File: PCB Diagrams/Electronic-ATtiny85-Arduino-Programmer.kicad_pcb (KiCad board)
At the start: 2 copper layers, 48.3 x 40.6 mm, 6 parts, among them J1 POWER, J2 01x03, J3 01x01, U1 Arduino Nano v3.x, U2 ATtiny85

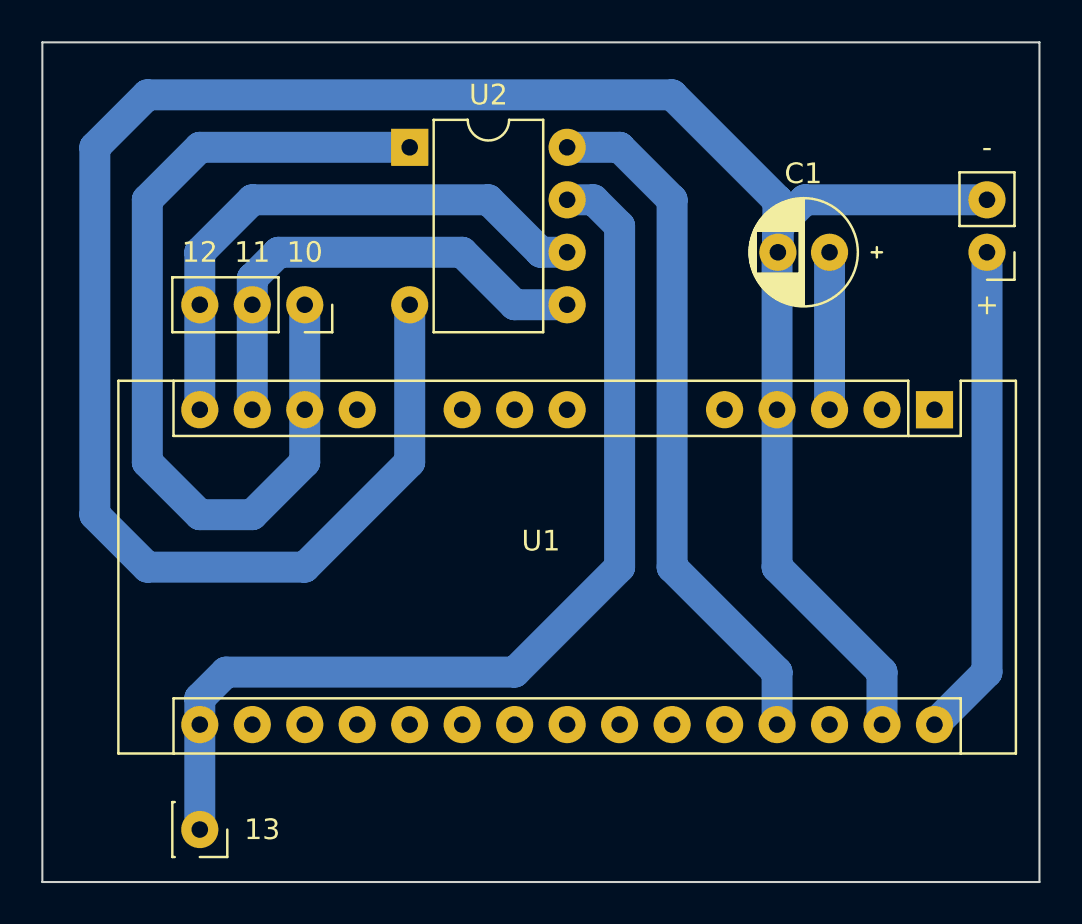
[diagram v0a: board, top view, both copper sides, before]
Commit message: optimizing PCB size
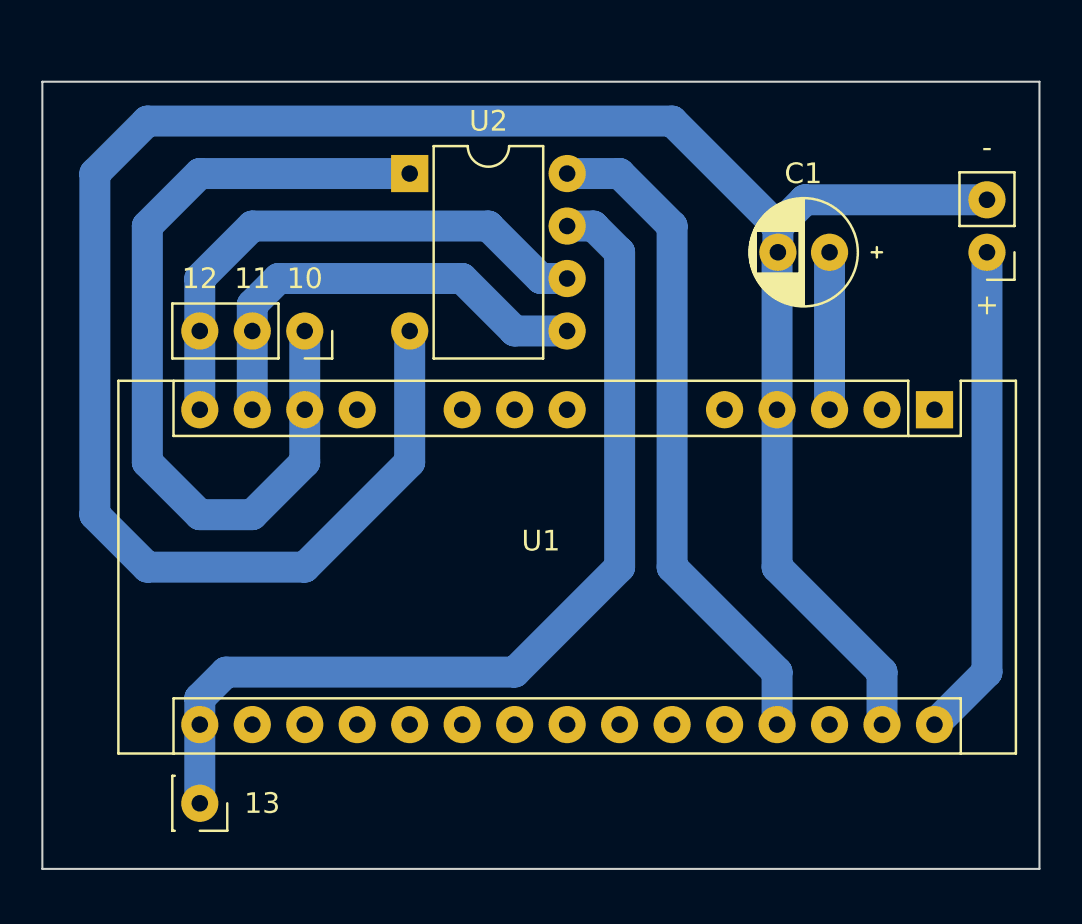
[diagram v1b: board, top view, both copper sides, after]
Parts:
- moved J2 1.27 mm to (137.2, 90.2)
- moved J3 1.27 mm to (132.1, 113.0)
- moved U2 1.27 mm to (142.2, 82.5)
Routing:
- net GND: track 119.4 -> 114.4 mm
- net Net-(J3-Pad1): track 48.9 -> 46.3 mm
- net Net-(J2-Pad1): track 43.8 -> 41.3 mm
- net Net-(J2-Pad2): track 23.2 -> 21.9 mm
- net Net-(J2-Pad3): track 27.5 -> 26.2 mm
- net Net-(U1-Pad27): track 33.6 -> 32.4 mm
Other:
- board size 48.3 x 40.6 mm -> 48.3 x 38.1 mm
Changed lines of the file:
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@@
   (net 26 "Net-(J3-Pad1)")
   (footprint "Connector_PinSocket_2.54mm:PinSocket_1x01_P2.54mm_Vertical" (layer "F.Cu")
-    (at 132.08 114.3 -90)
+    (at 132.08 113.03 -90)
     (descr "Through hole straight socket strip, 1x01, 2.54mm pitch, single row (from Kicad 4.0.7), script generated")
     (tags "Through hole socket strip THT 1x01 2.54mm single row")
@@
   )
   (footprint "Package_DIP:DIP-8_W7.62mm" (layer "F.Cu")
-    (at 142.24 81.28)
+    (at 142.24 82.55)
     (descr "8-lead though-hole mounted DIP package, row spacing 7.62 mm (300 mils)")
     (tags "THT DIP DIL PDIP 2.54mm 7.62mm 300mil")
@@
   )
   (footprint "Connector_PinSocket_2.54mm:PinSocket_1x03_P2.54mm_Vertical" (layer "F.Cu")
-    (at 137.16 88.9 -90)
+    (at 137.16 90.17 -90)
     (descr "Through hole straight socket strip, 1x03, 2.54mm pitch, single row (from Kicad 4.0.7), script generated")
     (tags "Through hole socket strip THT 1x03 2.54mm single row")
@@
     )
   )
-  (gr_line (start 124.46 76.2) (end 124.46 116.84) (layer "Edge.Cuts") (width 0.1))
-  (gr_line (start 172.72 76.2) (end 124.46 76.2) (layer "Edge.Cuts") (width 0.1))
-  (gr_line (start 124.46 116.84) (end 172.72 116.84) (layer "Edge.Cuts") (width 0.1))
-  (gr_line (start 172.72 116.84) (end 172.72 76.2) (layer "Edge.Cuts") (width 0.1))
-  (gr_text "12" (at 132.08 86.36) (layer "F.SilkS")
+  (gr_line (start 124.46 78.105) (end 124.46 116.205) (layer "Edge.Cuts") (width 0.1))
+  (gr_line (start 172.72 78.105) (end 124.46 78.105) (layer "Edge.Cuts") (width 0.1))
+  (gr_line (start 124.46 116.205) (end 172.72 116.205) (layer "Edge.Cuts") (width 0.1))
+  (gr_line (start 172.72 116.205) (end 172.72 78.105) (layer "Edge.Cuts") (width 0.1))
+  (gr_text "12" (at 132.08 87.63) (layer "F.SilkS")
     (effects (font (size 1 1) (thickness 0.2)))
   )
@@
     (effects (font (size 1 1) (thickness 0.2)))
   )
-  (gr_text "11" (at 134.62 86.36) (layer "F.SilkS")
+  (gr_text "11" (at 134.62 87.63) (layer "F.SilkS")
     (effects (font (size 1 1) (thickness 0.2)))
   )
@@
     (effects (font (size 1 1) (thickness 0.2)))
   )
-  (gr_text "13" (at 135.1 114.3) (layer "F.SilkS")
-    (effects (font (size 1 1) (thickness 0.2)))
-  )
-  (gr_text "10" (at 137.16 86.36) (layer "F.SilkS")
+  (gr_text "13" (at 135.1 113.03) (layer "F.SilkS")
+    (effects (font (size 1 1) (thickness 0.2)))
+  )
+  (gr_text "10" (at 137.16 87.63) (layer "F.SilkS")
     (effects (font (size 1 1) (thickness 0.2)))
   )
   (segment (start 162.56 93.98) (end 162.56 86.36) (width 1.5) (layer "B.Cu") (net 1))
   (segment (start 170.18 83.82) (end 161.367208 83.82) (width 1.5) (layer "B.Cu") (net 2))
-  (segment (start 129.54 78.74) (end 154.94 78.74) (width 1.5) (layer "B.Cu") (net 2))
+  (segment (start 127 99.06) (end 127 82.55) (width 1.5) (layer "B.Cu") (net 2))
+  (segment (start 129.54 80.01) (end 154.94 80.01) (width 1.5) (layer "B.Cu") (net 2))
   (segment (start 160.02 93.98) (end 160.02 86.4) (width 1.5) (layer "B.Cu") (net 2))
   (segment (start 161.367208 83.82) (end 160.06 85.127208) (width 1.5) (layer "B.Cu") (net 2))
-  (segment (start 160.06 83.86) (end 160.06 86.36) (width 1.5) (layer "B.Cu") (net 2))
   (segment (start 137.16 101.6) (end 129.54 101.6) (width 1.5) (layer "B.Cu") (net 2))
   (segment (start 160.06 85.127208) (end 160.06 86.36) (width 1.5) (layer "B.Cu") (net 2))
   (segment (start 129.54 101.6) (end 127 99.06) (width 1.5) (layer "B.Cu") (net 2))
-  (segment (start 154.94 78.74) (end 160.06 83.86) (width 1.5) (layer "B.Cu") (net 2))
-  (segment (start 127 81.28) (end 129.54 78.74) (width 1.5) (layer "B.Cu") (net 2))
+  (segment (start 154.94 80.01) (end 160.06 85.13) (width 1.5) (layer "B.Cu") (net 2))
+  (segment (start 127 82.55) (end 129.54 80.01) (width 1.5) (layer "B.Cu") (net 2))
   (segment (start 160.02 101.6) (end 160.02 93.98) (width 1.5) (layer "B.Cu") (net 2))
   (segment (start 165.1 106.68) (end 160.02 101.6) (width 1.5) (layer "B.Cu") (net 2))
-  (segment (start 142.24 88.9) (end 142.24 96.52) (width 1.5) (layer "B.Cu") (net 2))
+  (segment (start 142.24 90.17) (end 142.24 96.52) (width 1.5) (layer "B.Cu") (net 2))
   (segment (start 160.02 86.4) (end 160.06 86.36) (width 1.5) (layer "B.Cu") (net 2))
-  (segment (start 127 99.06) (end 127 81.28) (width 1.5) (layer "B.Cu") (net 2))
   (segment (start 165.1 109.22) (end 165.1 106.68) (width 1.5) (layer "B.Cu") (net 2))
   (segment (start 142.24 96.52) (end 137.16 101.6) (width 1.5) (layer "B.Cu") (net 2))
   (segment (start 170.18 106.68) (end 170.18 86.36) (width 1.5) (layer "B.Cu") (net 3))
   (segment (start 167.64 109.22) (end 170.18 106.68) (width 1.5) (layer "B.Cu") (net 3))
-  (segment (start 129.54 96.52) (end 129.54 83.82) (width 1.5) (layer "B.Cu") (net 4))
+  (segment (start 129.54 96.52) (end 129.54 85.09) (width 1.5) (layer "B.Cu") (net 4))
   (segment (start 137.16 93.98) (end 137.16 96.52) (width 1.5) (layer "B.Cu") (net 4))
-  (segment (start 129.54 83.82) (end 132.08 81.28) (width 1.5) (layer "B.Cu") (net 4))
+  (segment (start 129.54 85.09) (end 132.08 82.55) (width 1.5) (layer "B.Cu") (net 4))
   (segment (start 137.16 96.52) (end 134.62 99.06) (width 1.5) (layer "B.Cu") (net 4))
   (segment (start 134.62 99.06) (end 132.08 99.06) (width 1.5) (layer "B.Cu") (net 4))
-  (segment (start 137.16 88.9) (end 137.16 93.98) (width 1.5) (layer "B.Cu") (net 4))
-  (segment (start 132.08 81.28) (end 142.24 81.28) (width 1.5) (layer "B.Cu") (net 4))
+  (segment (start 137.16 90.17) (end 137.16 93.98) (width 1.5) (layer "B.Cu") (net 4))
+  (segment (start 132.08 82.55) (end 142.24 82.55) (width 1.5) (layer "B.Cu") (net 4))
   (segment (start 132.08 99.06) (end 129.54 96.52) (width 1.5) (layer "B.Cu") (net 4))
-  (segment (start 144.78 86.36) (end 135.887208 86.36) (width 1.5) (layer "B.Cu") (net 5))
-  (segment (start 134.62 87.627208) (end 135.887208 86.36) (width 1.5) (layer "B.Cu") (net 5))
-  (segment (start 147.32 88.9) (end 144.78 86.36) (width 1.5) (layer "B.Cu") (net 5))
+  (segment (start 144.78 87.63) (end 135.887208 87.63) (width 1.5) (layer "B.Cu") (net 5))
+  (segment (start 134.62 88.897208) (end 135.887208 87.63) (width 1.5) (layer "B.Cu") (net 5))
+  (segment (start 147.32 90.17) (end 144.78 87.63) (width 1.5) (layer "B.Cu") (net 5))
   (segment (start 134.62 88.9) (end 134.62 93.98) (width 1.5) (layer "B.Cu") (net 5))
-  (segment (start 149.86 88.9) (end 147.32 88.9) (width 1.5) (layer "B.Cu") (net 5))
-  (segment (start 134.62 88.9) (end 134.62 87.627208) (width 1.5) (layer "B.Cu") (net 5))
-  (segment (start 132.08 88.9) (end 132.08 93.98) (width 1.5) (layer "B.Cu") (net 6))
-  (segment (start 148.587208 86.36) (end 146.047208 83.82) (width 1.5) (layer "B.Cu") (net 6))
-  (segment (start 149.86 86.36) (end 148.587208 86.36) (width 1.5) (layer "B.Cu") (net 6))
-  (segment (start 146.047208 83.82) (end 134.62 83.82) (width 1.5) (layer "B.Cu") (net 6))
-  (segment (start 134.62 83.82) (end 132.08 86.36) (width 1.5) (layer "B.Cu") (net 6))
-  (segment (start 132.08 86.36) (end 132.08 88.9) (width 1.5) (layer "B.Cu") (net 6))
+  (segment (start 149.86 90.17) (end 147.32 90.17) (width 1.5) (layer "B.Cu") (net 5))
+  (segment (start 148.587208 87.63) (end 146.047208 85.09) (width 1.5) (layer "B.Cu") (net 6))
+  (segment (start 149.86 87.63) (end 148.587208 87.63) (width 1.5) (layer "B.Cu") (net 6))
+  (segment (start 146.047208 85.09) (end 134.62 85.09) (width 1.5) (layer "B.Cu") (net 6))
+  (segment (start 134.62 85.09) (end 132.08 87.63) (width 1.5) (layer "B.Cu") (net 6))
+  (segment (start 132.08 93.98) (end 132.08 87.63) (width 1.5) (layer "B.Cu") (net 6))
   (segment (start 154.94 101.6) (end 160.02 106.68) (width 1.5) (layer "B.Cu") (net 24))
-  (segment (start 154.94 83.82) (end 154.94 101.6) (width 1.5) (layer "B.Cu") (net 24))
-  (segment (start 152.4 81.28) (end 154.94 83.82) (width 1.5) (layer "B.Cu") (net 24))
-  (segment (start 149.86 81.28) (end 152.4 81.28) (width 1.5) (layer "B.Cu") (net 24))
+  (segment (start 154.94 101.6) (end 154.94 85.09) (width 1.5) (layer "B.Cu") (net 24))
+  (segment (start 152.4 82.55) (end 154.94 85.09) (width 1.5) (layer "B.Cu") (net 24))
+  (segment (start 149.86 82.55) (end 152.4 82.55) (width 1.5) (layer "B.Cu") (net 24))
   (segment (start 160.02 106.68) (end 160.02 109.22) (width 1.5) (layer "B.Cu") (net 24))
   (segment (start 147.32 106.68) (end 133.347208 106.68) (width 1.5) (layer "B.Cu") (net 26))
   (segment (start 152.4 101.6) (end 147.32 106.68) (width 1.5) (layer "B.Cu") (net 26))
   (segment (start 132.08 107.947208) (end 132.08 109.22) (width 1.5) (layer "B.Cu") (net 26))
-  (segment (start 151.132792 83.82) (end 152.4 85.087208) (width 1.5) (layer "B.Cu") (net 26))
-  (segment (start 149.86 83.82) (end 151.132792 83.82) (width 1.5) (layer "B.Cu") (net 26))
-  (segment (start 132.08 114.3) (end 132.08 109.22) (width 1.5) (layer "B.Cu") (net 26))
+  (segment (start 151.132792 85.09) (end 152.4 86.357208) (width 1.5) (layer "B.Cu") (net 26))
+  (segment (start 149.86 85.09) (end 151.132792 85.09) (width 1.5) (layer "B.Cu") (net 26))
+  (segment (start 132.08 109.22) (end 132.08 113.03) (width 1.5) (layer "B.Cu") (net 26))
   (segment (start 133.347208 106.68) (end 132.08 107.947208) (width 1.5) (layer "B.Cu") (net 26))
-  (segment (start 152.4 85.087208) (end 152.4 101.6) (width 1.5) (layer "B.Cu") (net 26))
+  (segment (start 152.4 101.6) (end 152.4 86.357208) (width 1.5) (layer "B.Cu") (net 26))
 )

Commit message: fixed PCB bug
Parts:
- added J2: 01x01, Connector_PinHeader_2.54mm:PinHeader_1x01_P2.54mm_Vertical, F.Cu at (154.9, 90.2)
- added J3: 01x02, Connector_PinHeader_2.54mm:PinHeader_1x02_P2.54mm_Vertical, F.Cu at (162.6, 90.2)
- C1: value 10uF/16V -> 10uF
- J1: value POWER -> PWR NANO
- J4: renamed from J2; footprint Connector_PinSocket_2.54mm:PinSocket_1x03_P2.54mm_Vertical -> Connector_PinHeader_2.54mm:PinHeader_1x03_P2.54mm_Vertical
- J5: renamed from J3; footprint Connector_PinSocket_2.54mm:PinSocket_1x01_P2.54mm_Vertical -> Connector_PinHeader_2.54mm:PinHeader_1x01_P2.54mm_Vertical
- moved C1 3.81 mm to (162.6, 82.5)
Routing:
- net GND: track 114.4 -> 118.9 mm
- net Net-(C1-Pad1): track 7.62 -> 11.4 mm
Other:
- board text added: "*"
- board text added: "5V"
- board text added: "GND"
- board text added: "RST"
